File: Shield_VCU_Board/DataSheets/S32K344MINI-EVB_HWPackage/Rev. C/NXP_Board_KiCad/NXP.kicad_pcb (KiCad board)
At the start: 2 copper layers, 160 x 63.4 mm, 8 parts

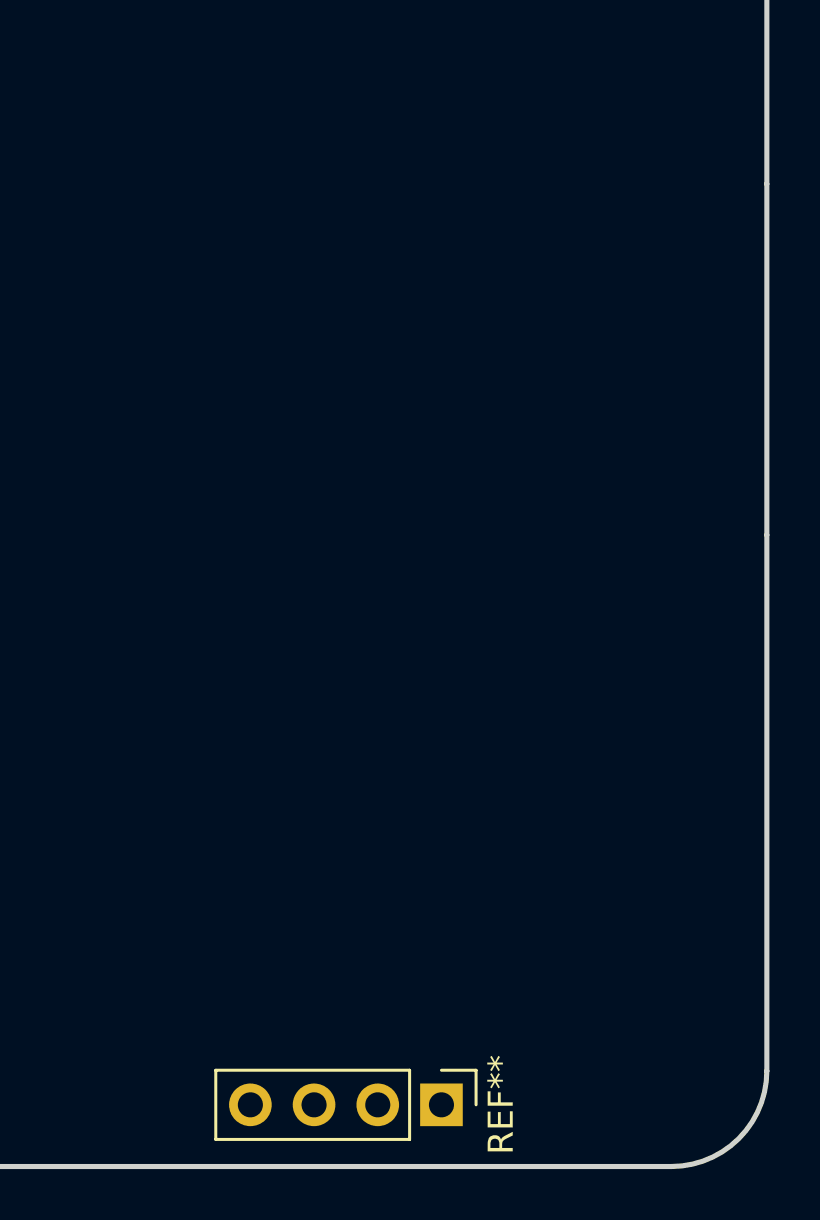
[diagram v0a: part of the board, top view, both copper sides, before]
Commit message: NXP_correction for3D_Enclosure
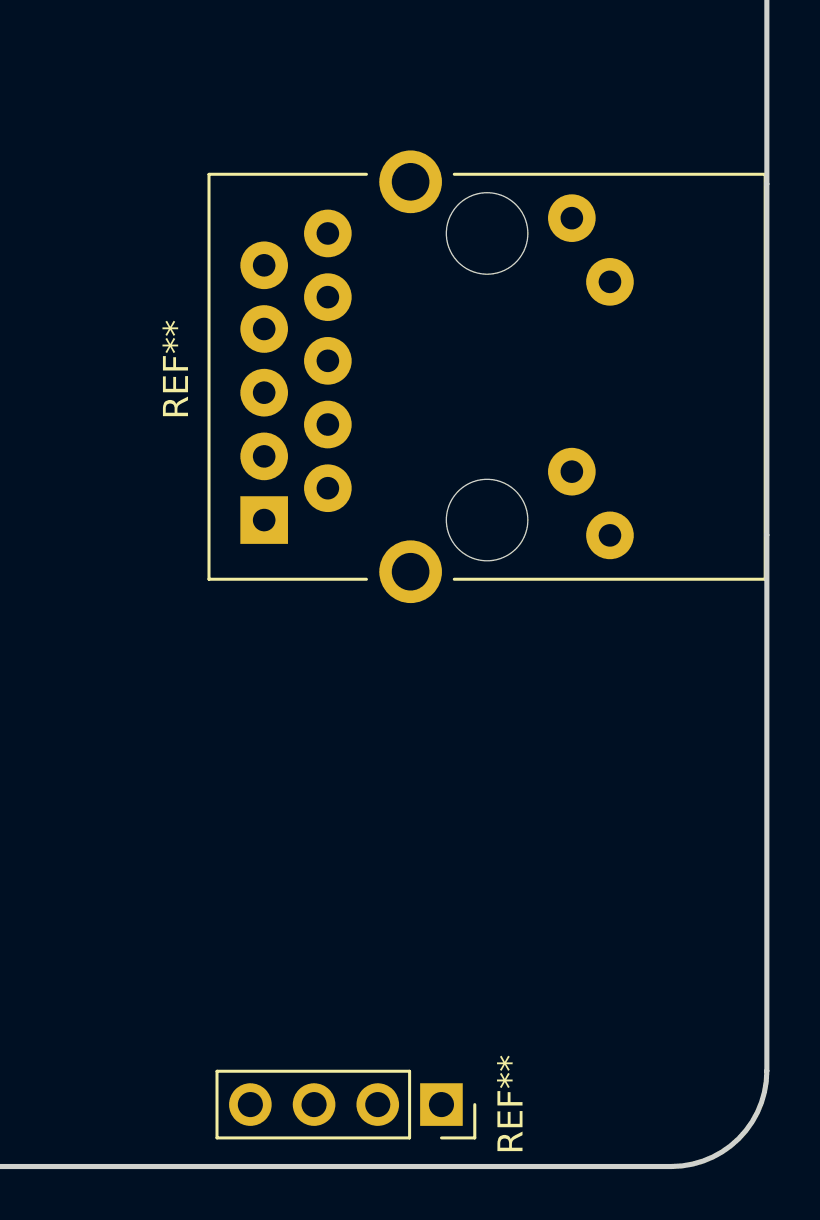
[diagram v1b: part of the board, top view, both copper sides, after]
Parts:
- removed the REF** at (215.7, 124.8)
- added REF**: RJ45_UDE_RB1-125B8G1A, Connector_RJ:RJ45_UDE_RB1-125B8G1A, F.Cu at (208.7, 101.5)
- added REF**: PinSocket_1x04_P2.54mm_Vertical, Connector_PinSocket_2.54mm:PinSocket_1x04_P2.54mm_Vertical, F.Cu at (215.7, 124.8)
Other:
- board text added: "BOTTOM"
- board text added: "Face TOP"
